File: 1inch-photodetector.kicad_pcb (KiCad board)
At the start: 4 copper layers, 25 x 25 mm, 21 parts, among them J1 Conn_01x03, J2 Conn_Coaxial, U1 ADA4898-2, U2 LT3032-12

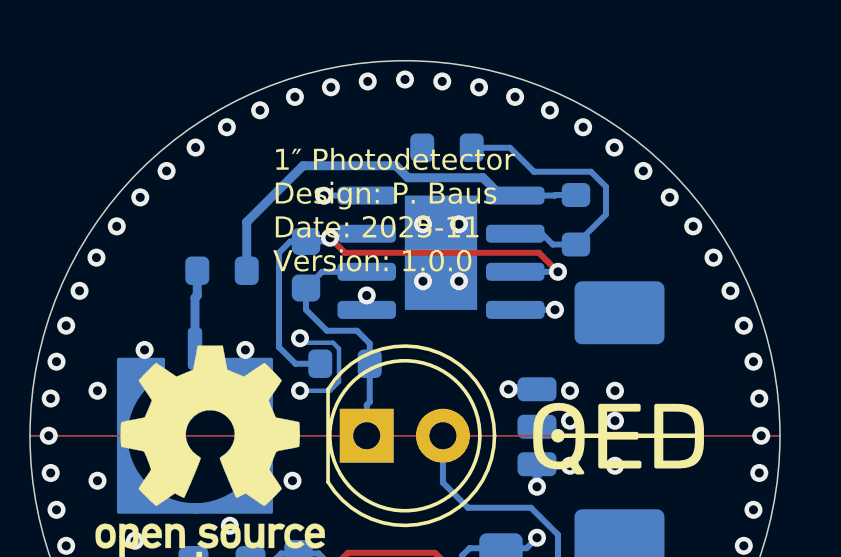
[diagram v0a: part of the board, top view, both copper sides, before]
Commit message: Added QED URL to version text
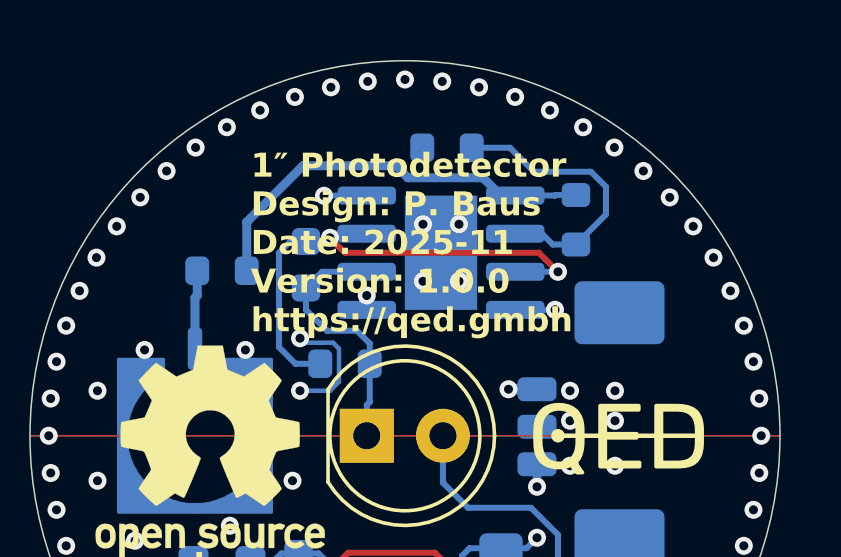
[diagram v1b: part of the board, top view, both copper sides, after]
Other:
- board text added: "1″ Photodetector Design: P. Baus Date: 2025-11 Version: 1.0.0 https://qed.gmbh"
- board text removed: "1″ Photodetector Design: P. Baus Date: 2025-11 Version: 1.0.0"
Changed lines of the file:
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@@
 		(layer "Edge.Cuts")
 	)
-	(gr_text "1″ Photodetector\nDesign: P. Baus\nDate: 2025-11\nVersion: 1.0.0"
-		(at 145.6 92.5 0)
+	(gr_text "1″ Photodetector\nDesign: P. Baus\nDate: 2025-11\nVersion: 1.0.0\nhttps://qed.gmbh"
+		(at 144.86 93.57 0)
 		(layer "F.SilkS")
 		(effects
 			(font
-				(size 0.7 0.7)
-				(thickness 0.1)
+				(size 0.8 0.8)
+				(thickness 0.16)
+				(bold yes)
 			)
 			(justify left)

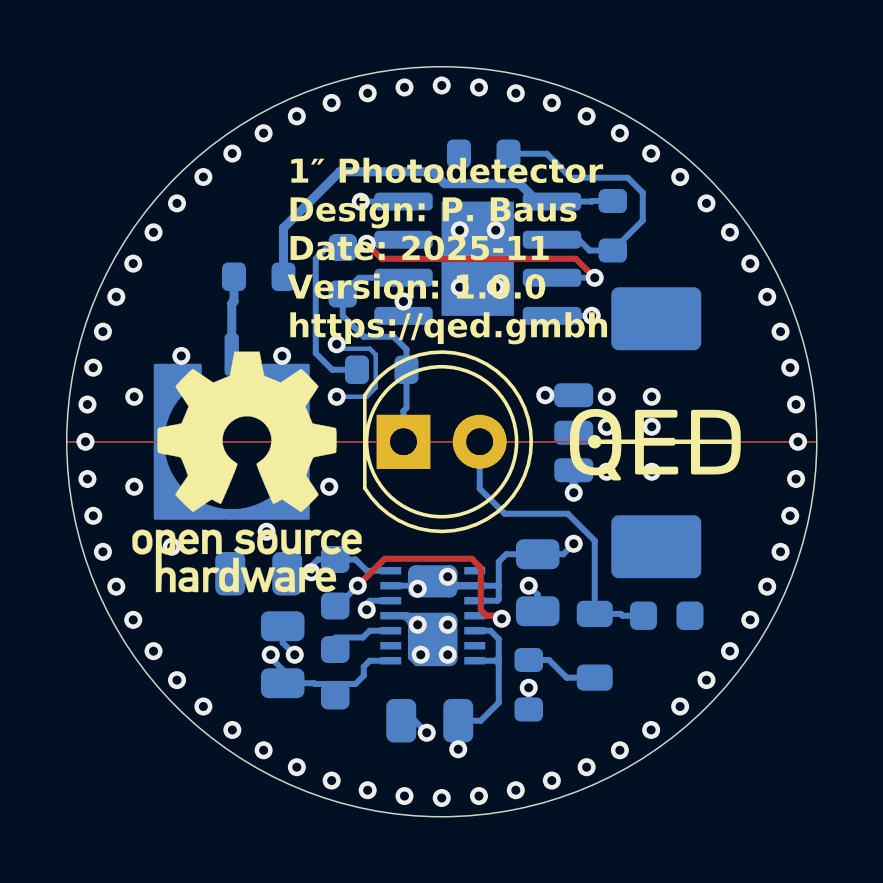
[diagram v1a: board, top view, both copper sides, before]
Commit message: Disconnect GND from Earth by default (#10)
* Removed GND-Earth connection
  - Added optional jumpers to connect GND to Earth
  - Added more ground stitching vias
* Increased size to 25.4 mm
* Added comments regarding tolerances
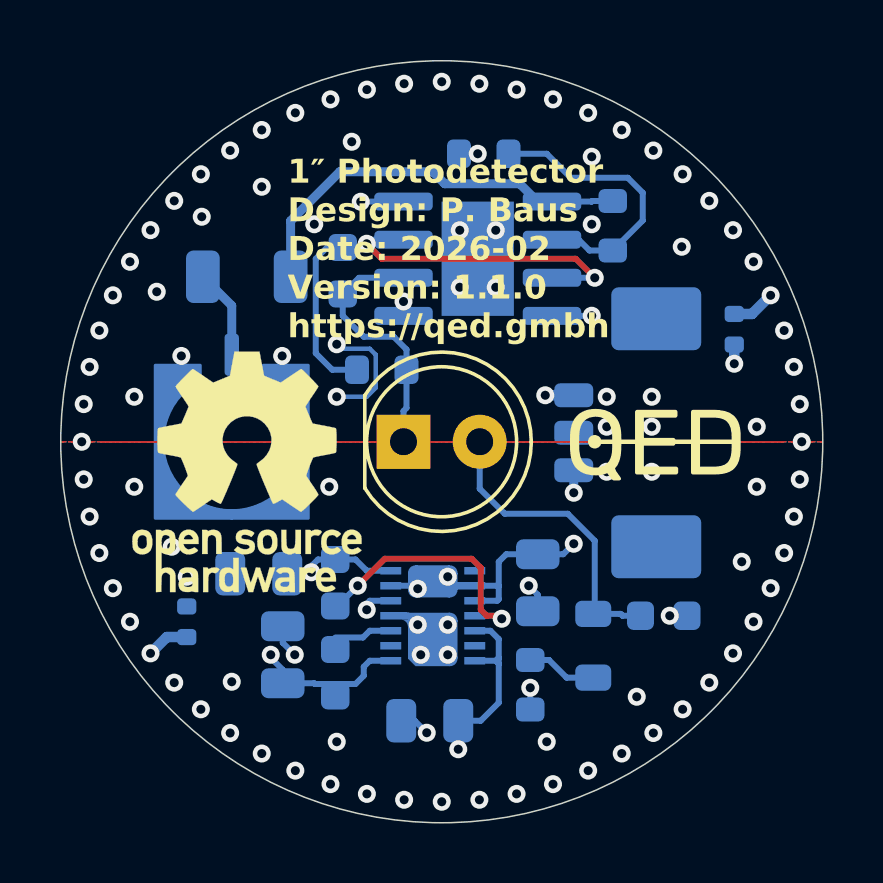
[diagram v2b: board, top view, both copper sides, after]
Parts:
- added JP1: Jumper_2_Open, Resistor_SMD:R_0402_1005Metric, B.Cu at (159.8, 96.2)
- added JP2: Jumper_2_Open, Resistor_SMD:R_0402_1005Metric, B.Cu at (141.5, 106.0)
- C3, C4: value C -> 100p
- C5, C6, C7, C8: value C -> 10u
- R1: footprint Resistor_SMD:R_0603_1608Metric -> Resistor_SMD:R_1206_3216Metric
- U2: value LT3032-12 -> LT3032IDE-12
- moved R1 0.40 mm to (143.5, 94.5)
- moved C2 0.10 mm to (157.4, 105.8)
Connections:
- net Net-(J1-Pin_1) renamed /V+
- net Net-(J1-Pin_3) renamed /V-
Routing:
- net Earth: track 0.00 -> 2.90 mm, vias 0 -> 60
- net GND: track 8.60 -> 10.4 mm, vias 84 -> 42
- added copper zone on B.Cu, net Earth
- added copper zone on F.Cu, net Earth
- added copper zone on In1.Cu, net Earth
- added copper zone on In2.Cu, net Earth
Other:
- board size 25 x 25 mm -> 25.4 x 25.4 mm
- board text added: "+"
- board text added: "-"
- board text added: "1″ Photodetector Design: P. Baus Date: 2026-02 Version: 1.1.0 https://qed.gmbh"
- board text added: "Clear aperture 22.9 mm (Thorlabs SM1RR retaining ring)"
- board text added: "G"
- board text removed: "1″ Photodetector Design: P. Baus Date: 2025-11 Version: 1.0.0 https://qed.gmbh"

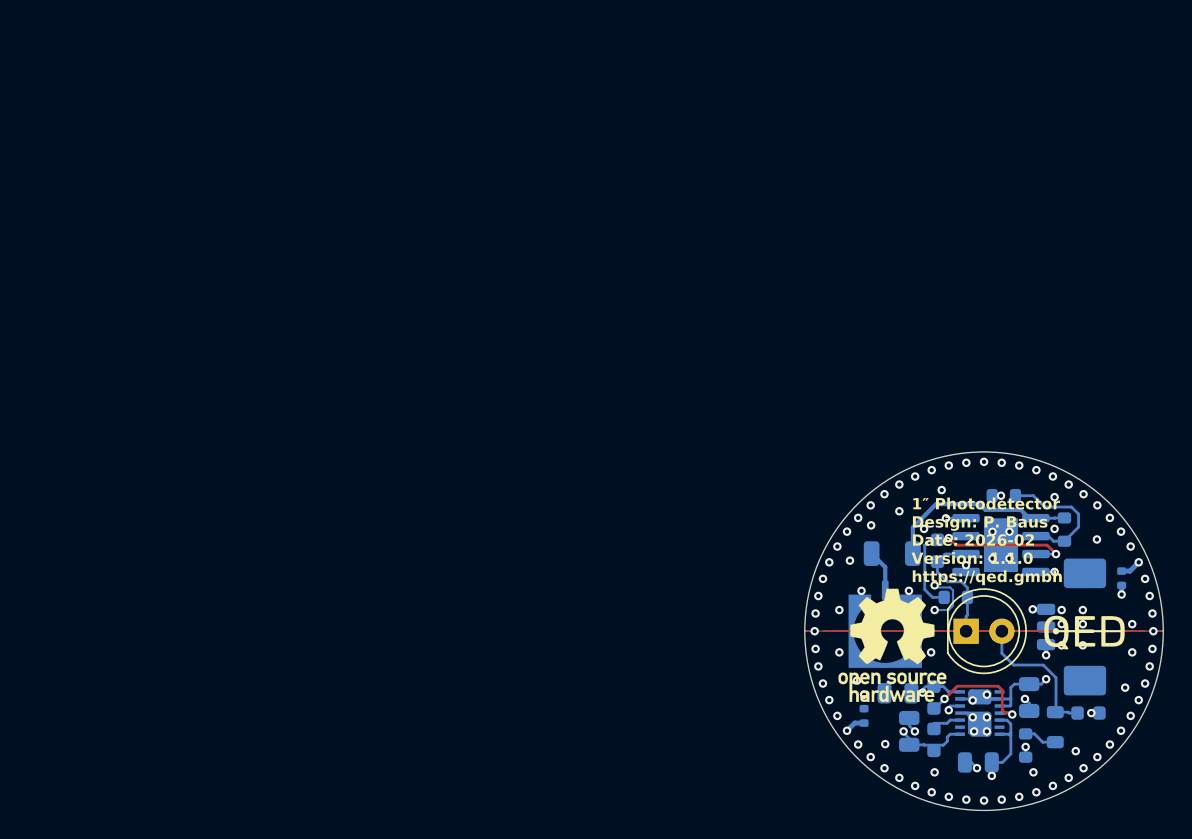
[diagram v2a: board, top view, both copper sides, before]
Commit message: Added stackup to gerber files
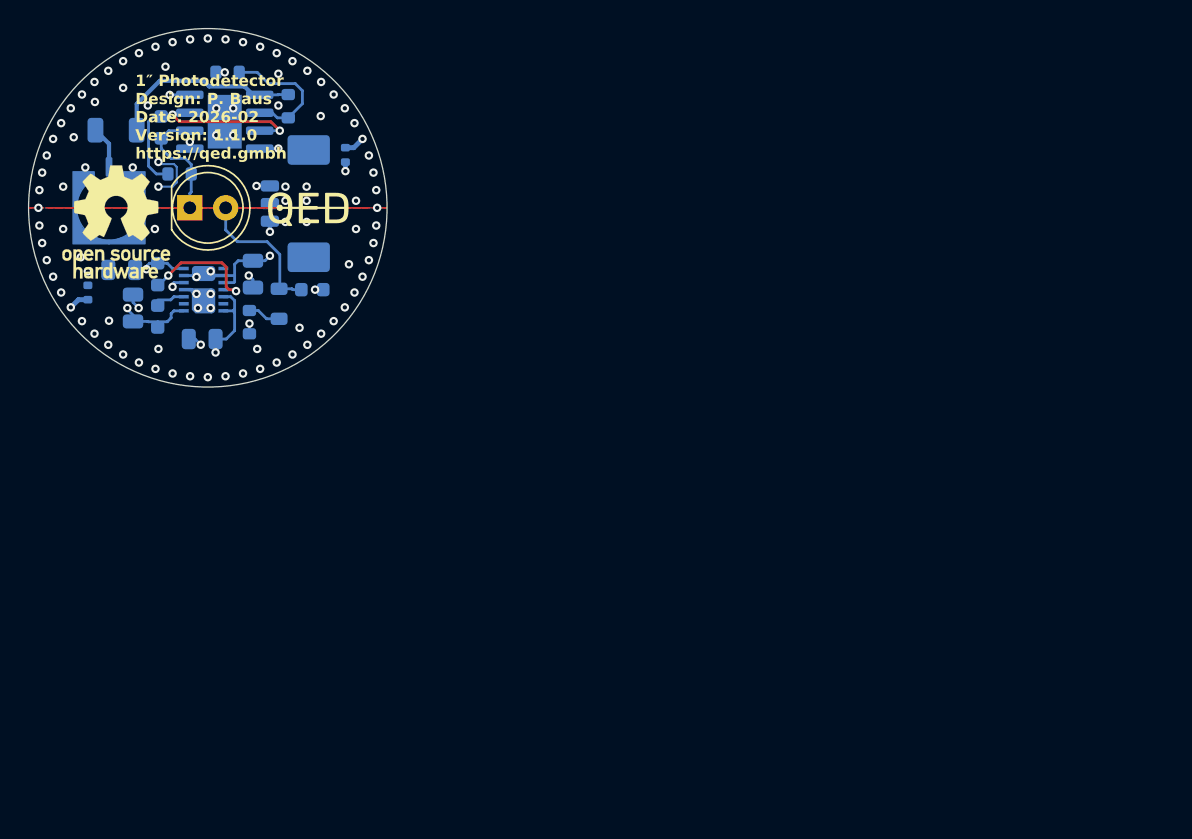
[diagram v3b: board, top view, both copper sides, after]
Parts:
- moved L1 62.6 mm to (100.0, 76.8)
- moved C2 62.6 mm to (102.4, 75.8)
- moved C6 62.6 mm to (94.6, 79.3)
- moved C8 62.6 mm to (88.9, 74.4)
- moved D1 62.6 mm to (93.7, 70.0)
- moved J1 62.6 mm to (100.7, 69.7)
- moved J2 62.6 mm to (88.0, 70.0)
- moved JP1 62.6 mm to (104.8, 66.2)
- moved JP2 62.6 mm to (86.5, 76.0)
- moved LOGO1 62.6 mm to (88.5, 71.0)
- moved R1 62.6 mm to (88.5, 64.5)
- moved R2 62.6 mm to (93.0, 67.6)
- moved R4 62.6 mm to (96.4, 60.4)
- moved SYM1 62.6 mm to (101.4, 70.0)
- moved U1 62.6 mm to (96.2, 63.9)
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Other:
- board text added: "0"
- board text added: "0 mm"
- board text added: "0,01 mm"
- board text added: "0,02"
- board text added: "0,035 mm"
- board text added: "0,1 mm"
- board text added: "0,1000 mm / 0,0000 mm"
- board text added: "0,2000 mm"
- board text added: "1"
- board text added: "1,24 mm"
- board text added: "1,6000 mm"
- board text added: "25,3975 mm x 25,3950 mm"
- board text added: "3,3"
- board text added: "4"
- board text added: "4,5"
- board text added: "B.Cu"
- board text added: "B.Mask"
- board text added: "B.Paste"
- board text added: "B.Silkscreen"
- board text added: "BOARD CHARACTERISTICS"
- board text added: "Black"
- board text added: "Board Thickness:"
- board text added: "Board overall dimensions:"
- board text added: "Bottom Silk Screen"
- board text added: "Bottom Solder Mask"
- board text added: "Bottom Solder Paste"
- board text added: "Castellated pads:"
- board text added: "Color"
- board text added: "Copper Finish:"
- board text added: "Copper Layer Count:"
- board text added: "Dielectric"
- board text added: "ENIG"
- board text added: "Edge card connectors:"
- board text added: "Epsilon R"
- board text added: "F.Cu"
- board text added: "F.Mask"
- board text added: "F.Paste"
- board text added: "F.Silkscreen"
- board text added: "FR4"
- board text added: "Impedance Control:"
- board text added: "In1.Cu"
- board text added: "In2.Cu"
- board text added: "Layer Name"
- board text added: "Loss Tangent"
- board text added: "Material"
- board text added: "Min hole diameter:"
- board text added: "Min track/spacing:"
- board text added: "No"
- board text added: "Not specified"
- board text added: "Plated Board Edge:"
- board text added: "Thickness (mm)"
- board text added: "Top Silk Screen"
- board text added: "Top Solder Mask"
- board text added: "Top Solder Paste"
- board text added: "Type"
- board text added: "White"
- board text added: "copper"
- board text added: "core"
- board text added: "prepreg"
